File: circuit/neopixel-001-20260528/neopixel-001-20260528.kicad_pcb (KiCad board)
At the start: 2 copper layers, 114.3 x 114.3 mm, 54 parts, among them J1 Conn_NeoPixel, P1 ESP32C3_{1}, P11 unitV4, P3 ESP32C3_{2}, P5 unitV1, P7 unitV2, P9 unitV3, SW1 SW_SPST, SW2 SW_SPST, SW3 SW_SPST, SW4 SW_SPST, U1 SSD1306

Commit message: Update ネオピク基板を進めた
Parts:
- moved C1 98.0 mm to (5.97, -30.0), turned to -11.25 degrees
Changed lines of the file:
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@@
 		(tags "LED RGB NeoPixel PLCC-4 5050")
 		(property "Reference" "D8"
-			(at 0 -3.5 -157.5)
+			(at 0 -3.5 202.5)
 			(unlocked yes)
 			(layer "F.Fab")
@@
 		)
 		(property "Value" "WS2812B"
-			(at 0 4.000001 -157.5)
+			(at 0 4.000001 202.5)
 			(unlocked yes)
 			(layer "F.Fab")
@@
 		)
 		(fp_text user "${REFERENCE}"
-			(at 0 0 -157.5)
+			(at 0 0 202.5)
 			(unlocked yes)
 			(layer "F.Fab")
@@
 		)
 		(fp_text user "1"
-			(at -4 -1.599999 -157.5)
+			(at -4 -1.599999 202.5)
 			(unlocked yes)
 			(layer "F.Fab")
@@
 		(tags "LED RGB NeoPixel PLCC-4 5050")
 		(property "Reference" "D2"
-			(at 0 -3.5 -22.5)
+			(at 0 -3.5 337.5)
 			(unlocked yes)
 			(layer "F.Fab")
@@
 		)
 		(property "Value" "WS2812B"
-			(at 0 4.000001 -22.5)
+			(at 0 4.000001 337.5)
 			(unlocked yes)
 			(layer "F.Fab")
@@
 		)
 		(fp_text user "1"
-			(at -4 -1.599999 -22.5)
+			(at -4 -1.599999 337.5)
 			(unlocked yes)
 			(layer "F.Fab")
@@
 		)
 		(fp_text user "${REFERENCE}"
-			(at 0 0 -22.5)
+			(at 0 0 337.5)
 			(unlocked yes)
 			(layer "F.Fab")
@@
 		(tags "LED RGB NeoPixel PLCC-4 5050")
 		(property "Reference" "D4"
-			(at 0 -3.5 -67.5)
+			(at 0 -3.5 292.5)
 			(unlocked yes)
 			(layer "F.Fab")
@@
 		)
 		(property "Value" "WS2812B"
-			(at 0 4.000001 -67.5)
+			(at 0 4.000001 292.5)
 			(unlocked yes)
 			(layer "F.Fab")
@@
 		)
 		(fp_text user "1"
-			(at -4 -1.599999 -67.5)
+			(at -4 -1.599999 292.5)
 			(unlocked yes)
 			(layer "F.Fab")
@@
 		)
 		(fp_text user "${REFERENCE}"
-			(at 0 0 -67.5)
+			(at 0 0 292.5)
 			(unlocked yes)
 			(layer "F.Fab")
@@
 		(tags "LED RGB NeoPixel PLCC-4 5050")
 		(property "Reference" "D5"
-			(at 0 -3.5 -90)
+			(at 0 -3.5 270)
 			(unlocked yes)
 			(layer "F.Fab")
@@
 		)
 		(property "Value" "WS2812B"
-			(at 0 4 -90)
+			(at 0 4 270)
 			(unlocked yes)
 			(layer "F.Fab")
@@
 		)
 		(fp_text user "${REFERENCE}"
-			(at 0 0 -90)
+			(at 0 0 270)
 			(unlocked yes)
 			(layer "F.Fab")
@@
 		)
 		(fp_text user "1"
-			(at -4 -1.6 -90)
+			(at -4 -1.6 270)
 			(unlocked yes)
 			(layer "F.Fab")
@@
 		(tags "LED RGB NeoPixel PLCC-4 5050")
 		(property "Reference" "D3"
-			(at 0 -3.499999 -45)
+			(at 0 -3.499999 315)
 			(unlocked yes)
 			(layer "F.Fab")
@@
 		)
 		(property "Value" "WS2812B"
-			(at 0 4.000001 -45)
+			(at 0 4.000001 315)
 			(unlocked yes)
 			(layer "F.Fab")
@@
 		)
 		(fp_text user "1"
-			(at -4 -1.599999 -45)
+			(at -4 -1.599999 315)
 			(unlocked yes)
 			(layer "F.Fab")
@@
 		)
 		(fp_text user "${REFERENCE}"
-			(at 0 0 -45)
+			(at 0 0 315)
 			(unlocked yes)
 			(layer "F.Fab")
@@
 		(tags "LED RGB NeoPixel PLCC-4 5050")
 		(property "Reference" "D7"
-			(at 0 -3.499999 -135)
+			(at 0 -3.499999 225)
 			(unlocked yes)
 			(layer "F.Fab")
@@
 		)
 		(property "Value" "WS2812B"
-			(at 0 4.000001 -135)
+			(at 0 4.000001 225)
 			(unlocked yes)
 			(layer "F.Fab")
@@
 		)
 		(fp_text user "${REFERENCE}"
-			(at 0 0 -135)
+			(at 0 0 225)
 			(unlocked yes)
 			(layer "F.Fab")
@@
 		)
 		(fp_text user "1"
-			(at -4 -1.599999 -135)
+			(at -4 -1.599999 225)
 			(unlocked yes)
 			(layer "F.Fab")
@@
 	(footprint "Capacitor_SMD:C_0805_2012Metric"
 		(layer "F.Cu")
-		(at 93.915 13.295)
+		(at 5.970447 -30.015462 -11.25)
 		(descr "Capacitor SMD 0805 (2012 Metric), square (rectangular) end terminal, IPC-7351 nominal, (Body size source: IPC-SM-782 page 76, https://www.pcb-3d.com/wordpress/wp-content/uploads/ipc-sm-782a_amendment_1_and_2.pdf, https://docs.google.com/spreadsheets/d/1BsfQQcO9C6DZCsRaXUlFlo91Tg2WpOkGARC1WS5S8t0/edit?usp=sharing)")
 		(tags "capacitor")
 		(property "Reference" "C1"
-			(at 0 -1.68 0)
+			(at 0 -1.68 168.75)
 			(layer "F.SilkS")
 			(effects
@@
 		)
 		(property "Value" "100n"
-			(at 0 1.68 0)
+			(at 0 1.68 168.75)
 			(layer "F.Fab")
 			(effects
@@
 		)
 		(property "Datasheet" ""
-			(at 0 0 0)
+			(at 0 0 168.75)
 			(layer "F.Fab")
 			(hide yes)
@@
 		)
 		(property "Description" ""
-			(at 0 0 0)
+			(at 0 0 168.75)
 			(layer "F.Fab")
 			(hide yes)
@@
 		)
 		(property "KiLib_Generator" "SMD_2terminal_chip_molded"
-			(at 0 0 0)
+			(at 0 0 168.75)
 			(layer "F.SilkS")
 			(hide yes)
@@
 		(duplicate_pad_numbers_are_jumpers no)
 		(fp_line
-			(start -0.261252 -0.735)
-			(end 0.261252 -0.735)
+			(start -0.261253 0.735)
+			(end 0.261252 0.735)
 			(stroke
 				(width 0.12)
@@
 		)
 		(fp_line
-			(start -0.261252 0.735)
-			(end 0.261252 0.735)
+			(start -0.261252 -0.735)
+			(end 0.261253 -0.735)
 			(stroke
 				(width 0.12)
@@
 			(layer "F.SilkS")
 		)
-		(fp_rect
-			(start -1.7 -0.98)
-			(end 1.7 0.98)
+		(fp_poly
+			(pts
+				(xy -1.7 -0.98) (xy 1.7 -0.98) (xy 1.7 0.98) (xy -1.7 0.98)
+			)
 			(stroke
 				(width 0.05)
@@
 			(layer "F.CrtYd")
 		)
-		(fp_rect
-			(start -1 -0.625)
-			(end 1 0.625)
+		(fp_poly
+			(pts
+				(xy -1 -0.625) (xy 1 -0.625) (xy 1 0.625) (xy -1 0.625)
+			)
 			(stroke
 				(width 0.1)
@@
 		)
 		(fp_text user "${REFERENCE}"
-			(at 0 0 0)
+			(at 0 0 168.75)
 			(layer "F.Fab")
 			(effects
@@
 		)
 		(pad "1" smd roundrect
-			(at -0.95 0)
+			(at -0.95 0 348.75)
 			(size 1 1.45)
 			(layers "F.Cu" "F.Mask" "F.Paste")
@@
 		)
 		(pad "2" smd roundrect
-			(at 0.95 0)
+			(at 0.95 0 348.75)
 			(size 1 1.45)
 			(layers "F.Cu" "F.Mask" "F.Paste")
@@
 		(tags "LED RGB NeoPixel PLCC-4 5050")
 		(property "Reference" "D6"
-			(at 0 -3.5 -112.5)
+			(at 0 -3.5 247.5)
 			(unlocked yes)
 			(layer "F.Fab")
@@
 		)
 		(property "Value" "WS2812B"
-			(at 0 4.000001 -112.5)
+			(at 0 4.000001 247.5)
 			(unlocked yes)
 			(layer "F.Fab")
@@
 		)
 		(fp_text user "${REFERENCE}"
-			(at 0 0 -112.5)
+			(at 0 0 247.5)
 			(unlocked yes)
 			(layer "F.Fab")
@@
 		)
 		(fp_text user "1"
-			(at -4 -1.599999 -112.5)
+			(at -4 -1.599999 247.5)
 			(unlocked yes)
 			(layer "F.Fab")

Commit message: Update ネオピクセル基板の部品を一旦配置してみた
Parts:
- added J2: Conn_01x02_Pin, Connector_JST:JST_XH_B2B-XH-A_1x02_P2.50mm_Vertical, B.Cu at (-31.5, -39.0)
- added J3: Conn_01x02_Pin, Connector_JST:JST_XH_B2B-XH-A_1x02_P2.50mm_Vertical, B.Cu at (-39.5, -32.0)
- added P10: unitV3, @Thrive_footprint_neopixel:USB_Type-C_Vertical_ C6332304, B.Cu at (10.0, 34.0)
- added P12: unitV4, @Thrive_footprint_neopixel:USB_Type-C_Vertical_ C6332304, B.Cu at (35.5, 6.67)
- added P2: ESP32C3_{1}, @Thrive_footprint_neopixel:USB_Type-C_Vertical_ C6332304, B.Cu at (-39.0, 14.0)
- added P4: ESP32C3_{2}, @Thrive_footprint_neopixel:USB_Type-C_Vertical_ C6332304, B.Cu at (39.0, 14.0)
- added P6: unitV1, @Thrive_footprint_neopixel:USB_Type-C_Vertical_ C6332304, B.Cu at (-42.0, 7.00)
- added P8: unitV2, @Thrive_footprint_neopixel:USB_Type-C_Vertical_ C6332304, B.Cu at (-10.0, 34.0)
- added R10: 330, Resistor_SMD:R_0805_2012Metric, B.Cu at (43.0, 0.00)
- added R7: 10k, Resistor_SMD:R_0805_2012Metric, B.Cu at (15.0, 42.0)
- added R8: 330, Resistor_SMD:R_0805_2012Metric, B.Cu at (15.0, 40.0)
- added R9: 10k, Resistor_SMD:R_0805_2012Metric, B.Cu at (45.0, 0.00)
- added U2: Aexit_0-50_Voltmeter, @Thrive_footprint_neopixel:Aexit_0-50_Voltmeter, F.Cu at (0.00, -44.0)
- C1, C10, C11, C12, C13, C14, C15, C16, C17, C18, C19, C2, C20, C3, C4, C5, C6, C7, C8, C9, R1, R2, R3, R5: moved to B.Cu
- J1: footprint Connector_FFC-FPC:JUSHUO_AFA07-S12FCA-00_1x12-1MP_P1.0mm_Horizontal -> @Thrive_footprint_neopixel:AFC01-S12FCA-00; moved to B.Cu
- R4, R6: value 10k -> 330; moved to B.Cu
- SW1, SW2, SW3, SW4: value SW_SPST -> SW_SPST_LED
- moved R2 151.7 mm to (-39.0, -1.00), turned to 180 degrees
- moved R1 151.1 mm to (-39.0, 2.00), turned to 180 degrees
- moved C14 135.4 mm to (-28.3, -11.7), turned to -112.5 degrees
- moved C13 134.8 mm to (-30.6, 0.00), turned to -90 degrees
- moved C15 133.0 mm to (-21.6, -21.6), turned to -135 degrees
- moved C12 131.2 mm to (-28.3, 11.7), turned to -67.5 degrees
- moved R3 128.7 mm to (-15.0, 42.0), turned to 180 degrees
- moved R4 128.0 mm to (-15.0, 40.0), turned to 180 degrees
- moved C16 126.0 mm to (-11.7, -28.3), turned to -157.5 degrees
- moved C17 125.4 mm to (-15.0, 44.0)
- moved C11 124.7 mm to (-21.6, 21.6), turned to -45 degrees
- moved R5 113.0 mm to (0.00, 42.0), turned to 180 degrees
- moved R6 112.3 mm to (0.00, 40.0), turned to 180 degrees
- moved C10 110.1 mm to (-11.7, 28.3), turned to -22.5 degrees
- moved C18 110.1 mm to (0.00, 44.0)
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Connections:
- C20 pad 2: SW_{TCT4} -> SW_{START}
- J1 pad 11: SW_{TCT4} -> SW_{START}
- R4 pad 1: SW_{TCT2} -> Net-(SW1-A)
- R5 pad 1: SW_{TCT3} -> SW_{TCT2}
- R6 pad 1: SW_{TCT4} -> Net-(SW2-A)
- SW1 pad 3: (no net) -> GND
- SW1 pad 4: (no net) -> Net-(SW1-A)
- SW2 pad 3: (no net) -> GND
- SW2 pad 4: (no net) -> Net-(SW2-A)
- SW3 pad 3: (no net) -> GND
- SW3 pad 4: (no net) -> Net-(SW3-A)
- SW4 pad 2: SW_{TCT4} -> SW_{START}
- SW4 pad 3: (no net) -> GND
- SW4 pad 4: (no net) -> Net-(SW4-A)

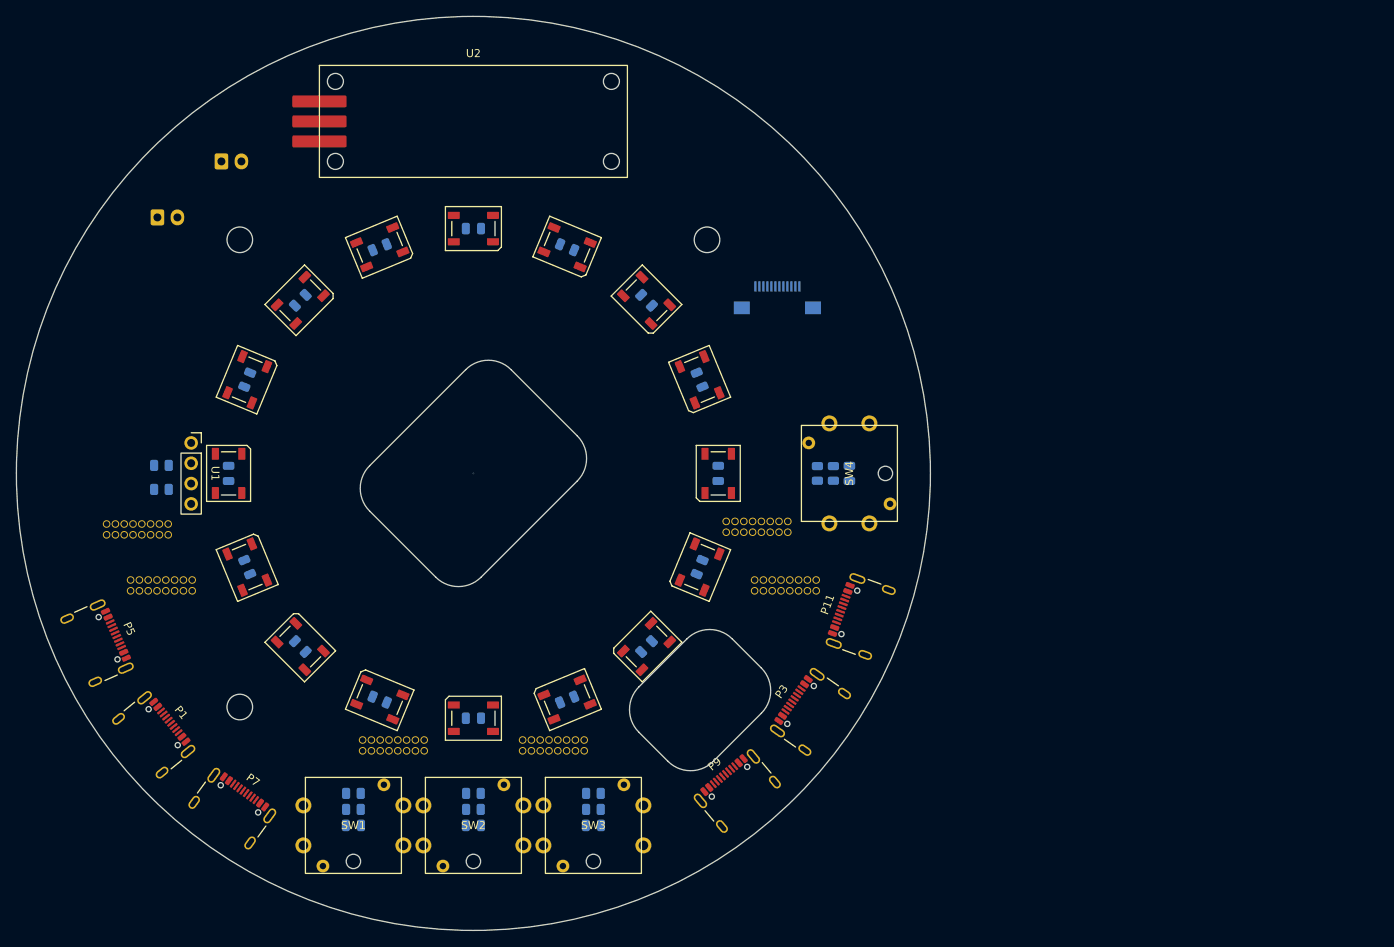
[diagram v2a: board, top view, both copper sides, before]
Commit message: Update ネオピクセル基板の部品配置した
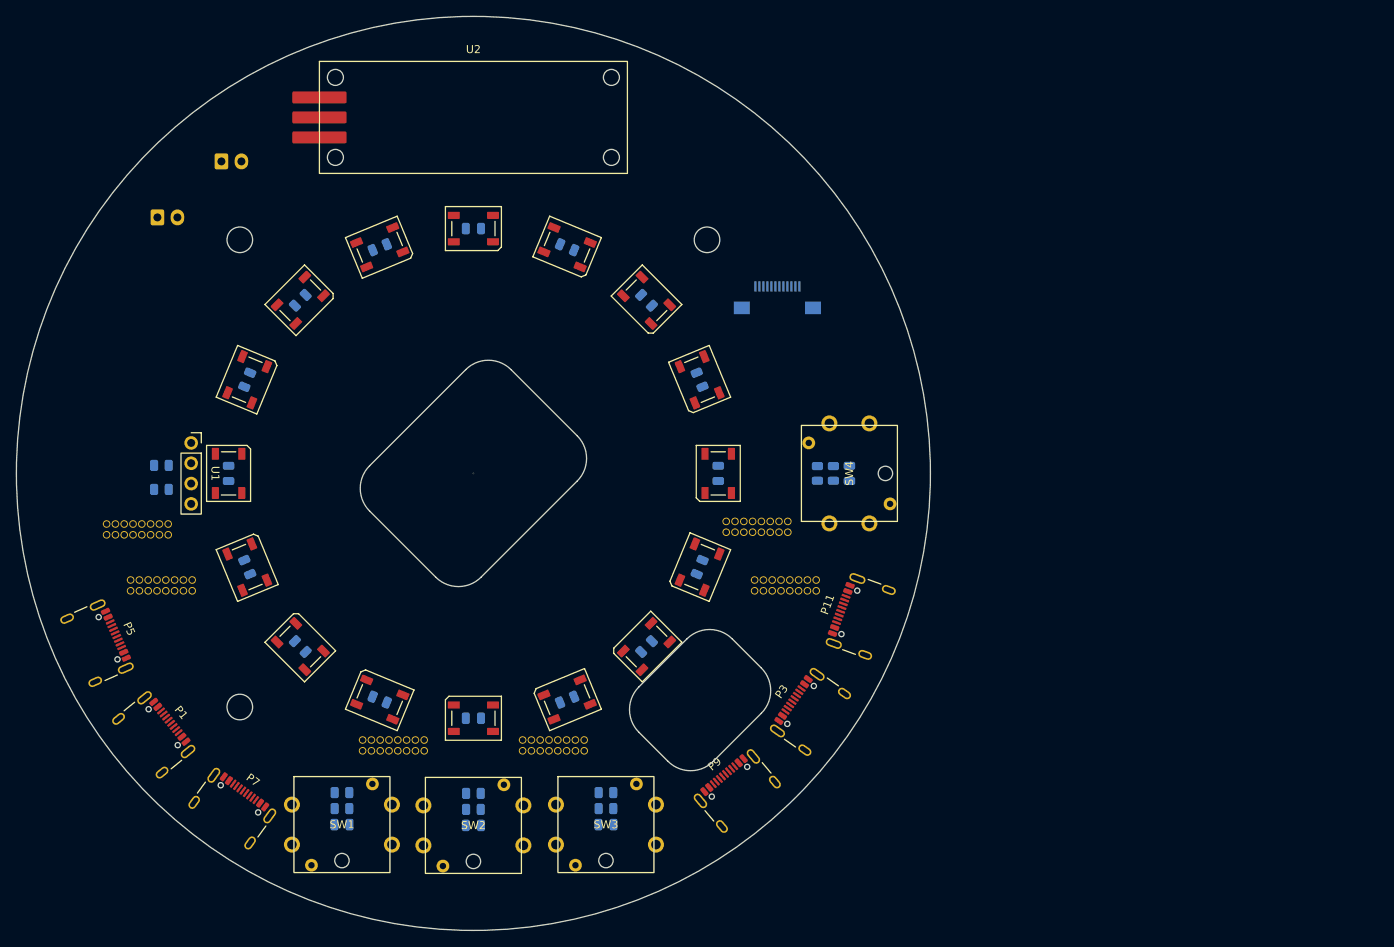
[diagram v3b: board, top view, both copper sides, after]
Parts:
- moved C19 1.57 mm to (16.6, 43.9)
- moved R7 1.57 mm to (16.6, 41.9)
- moved R8 1.57 mm to (16.6, 39.9)
- moved SW3 1.57 mm to (16.6, 43.9)
- moved C17 1.44 mm to (-16.4, 43.9)
- moved R3 1.44 mm to (-16.4, 41.9)
- moved R4 1.44 mm to (-16.4, 39.9)
- moved SW1 1.44 mm to (-16.4, 43.9)
- moved U2 0.50 mm to (0.00, -44.5)

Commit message: Update ネオピク基板のPCBを進めてる。差動をどう配線すればいいんや
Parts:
- turned C1 to 0 degrees
- turned C10 to 157.5 degrees
- turned C11 to 135 degrees
- turned C12 to 112.5 degrees
- turned C13 to 90 degrees
- turned C14 to 67.5 degrees
- turned C15 to 45 degrees
- turned C16 to 22.5 degrees
- turned C2 to -22.5 degrees
- turned C3 to -45 degrees
- turned C4 to -67.5 degrees
- turned C5 to -90 degrees
- turned C6 to -112.5 degrees
- turned C7 to -135 degrees
- turned C8 to -157.5 degrees
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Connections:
- net Net-(P1-CC) renamed P1_CC
- net Net-(P1-D+) renamed P1_D-
- net Net-(P1-D-) renamed P1_D+
- net Net-(P1-SBU1) renamed P1_SBU1
- net Net-(P1-SBU2) renamed P1_SBU2
- net Net-(P1-VBUS-PadA4) renamed P1_VBUS
- net Net-(P1-VCONN) renamed P1_VCONN
- net Net-(P10-CC) renamed P5_CC
- net Net-(P10-D+) renamed P5_D-
- net Net-(P10-D-) renamed P5_D+
- net Net-(P10-SBU1) renamed P5_SBU1
- net Net-(P10-SBU2) renamed P5_SBU2
- net Net-(P10-VBUS-PadA4) renamed P5_VBUS
- net Net-(P10-VCONN) renamed P5_VCONN
- net Net-(P11-CC) renamed P6_CC
- net Net-(P11-D+) renamed P6_D-
- net Net-(P11-D-) renamed P6_D+
- net Net-(P11-SBU1) renamed P6_SBU1
- net Net-(P11-SBU2) renamed P6_SBU2
- net Net-(P11-VBUS-PadA4) renamed P6_VBUS
- net Net-(P11-VCONN) renamed P6_VCONN
- net Net-(P3-CC) renamed P2_CC
- net Net-(P3-D+) renamed P2_D-
- net Net-(P3-D-) renamed P2_D+
- net Net-(P3-SBU1) renamed P2_SBU1
- net Net-(P3-SBU2) renamed P2_SBU2
- net Net-(P3-VBUS-PadA4) renamed P2_VBUS
- net Net-(P3-VCONN) renamed P2_VCONN
- net Net-(P5-CC) renamed P3_CC
- net Net-(P5-D+) renamed P3_D-
- net Net-(P5-D-) renamed P3_D+
- net Net-(P5-SBU1) renamed P3_SBU1
- net Net-(P5-SBU2) renamed P3_SBU2
- net Net-(P5-VBUS-PadA4) renamed P3_VBUS
- net Net-(P5-VCONN) renamed P3_VCONN
- net Net-(P7-CC) renamed P4_CC
- net Net-(P7-D+) renamed P4_D-
- net Net-(P7-D-) renamed P4_D+
- net Net-(P7-SBU1) renamed P4_SBU1
- net Net-(P7-SBU2) renamed P4_SBU2
- net Net-(P7-VBUS-PadA4) renamed P4_VBUS
- net Net-(P7-VCONN) renamed P4_VCONN
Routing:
- net GND: track 0.00 -> 80.1 mm, vias 0 -> 16
- net +5V: track 0.00 -> 50.5 mm, vias 0 -> 16
- net P3_VBUS: track 0.00 -> 36.6 mm
- net +48V: track 0.00 -> 31.1 mm
- net P3_D+: track 0.00 -> 24.0 mm
- net P3_D-: track 0.00 -> 23.3 mm
- net (no net): track 0.00 -> 7.79 mm
- net P3_CC: track 0.00 -> 4.92 mm
- net P3_SBU1: track 0.00 -> 2.21 mm
- net P3_VCONN: track 0.00 -> 2.12 mm
- net P3_SBU2: track 0.00 -> 1.80 mm
